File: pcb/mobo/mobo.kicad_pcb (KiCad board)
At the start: 2 copper layers, 51.6 x 89 mm, 70 parts, among them J1 ISP, J2 PEEL_MOTOR, J3 DRIVE_MOTOR, J4 SW1, J5 SPRING_FINGERS, J6 SW2, J8 USART1, U1 ATmega328P-A, U2 ATmega328P-M, U4 AP1117-50, U5 MC34063AD, U6 SP308xE, U7 DRV8837, U8 DRV8837, Y1 16MHz

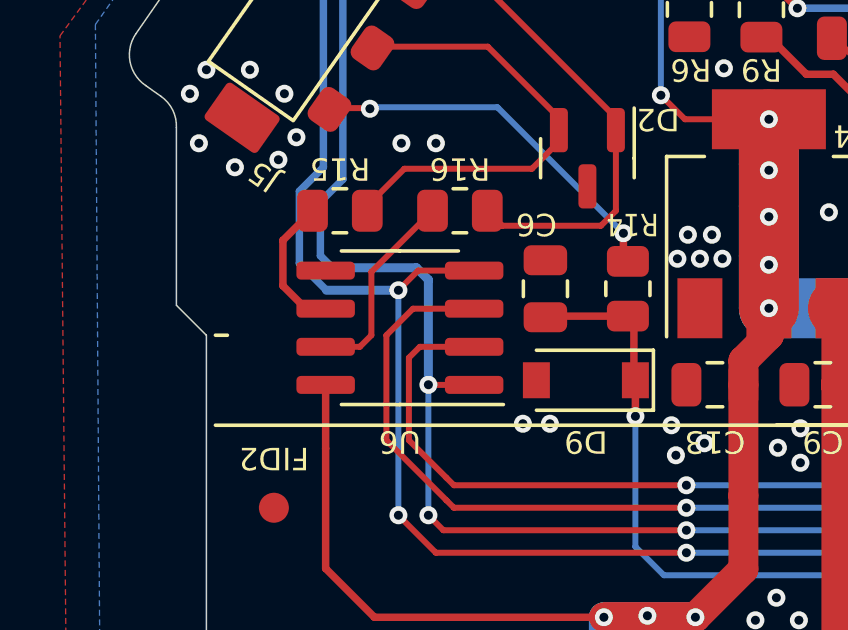
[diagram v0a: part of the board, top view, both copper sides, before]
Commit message: Add decoupling cap for RS-485 transceiver, Set edge clearance to 0.2mm
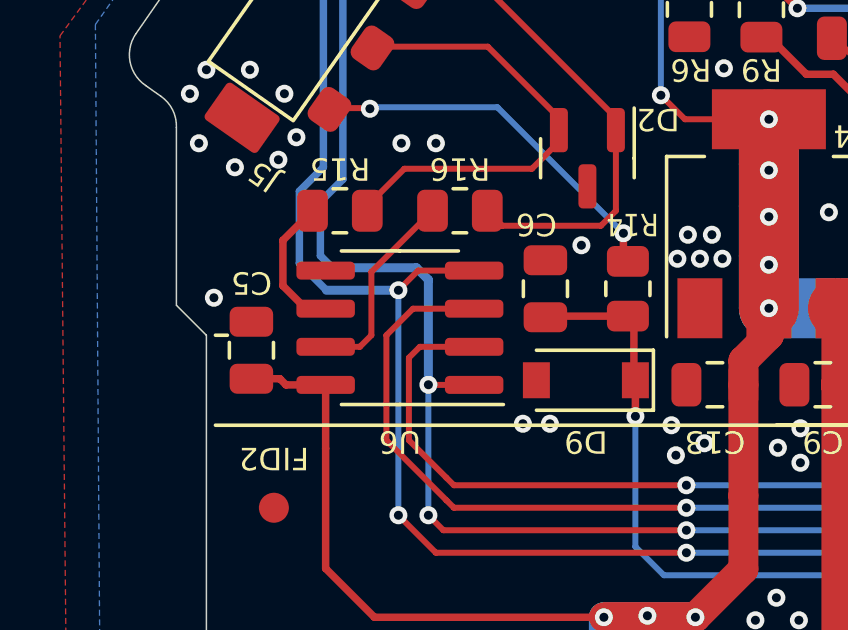
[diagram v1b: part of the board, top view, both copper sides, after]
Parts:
- added C5: 100n, Capacitor_SMD:C_0805_2012Metric, F.Cu at (103.8, 50.3)
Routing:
- net +5V: track 244.5 -> 247.0 mm
- net GND: vias 115 -> 117
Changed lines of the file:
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@@
     )
   )
+  (footprint "Capacitor_SMD:C_0805_2012Metric" (layer "F.Cu")
+    (at 103.8 50.3 -90)
+    (descr "Capacitor SMD 0805 (2012 Metric), square (rectangular) end terminal, IPC_7351 nominal, (Body size source: IPC-SM-782 page 76, https://www.pcb-3d.com/wordpress/wp-content/uploads/ipc-sm-782a_amendment_1_and_2.pdf, https://docs.google.com/spreadsheets/d/1BsfQQcO9C6DZCsRaXUlFlo91Tg2WpOkGARC1WS5S8t0/edit?usp=sharing), generated with kicad-footprint-generator")
+    (tags "capacitor")
+    (property "JLCPCB" "C49678")
+    (property "LCSC" "C476766")
+    (property "Sheetfile" "mobo.kicad_sch")
+    (property "Sheetname" "")
+    (property "ki_description" "Unpolarized capacitor, small symbol")
+    (property "ki_keywords" "capacitor cap")
+    (attr smd)
+    (fp_text reference "C5" (at -2.25 0 -180 unlocked) (layer "F.SilkS")
+        (effects (font (size 0.75 0.75) (thickness 0.1)))
+    )
+    (fp_text value "100n" (at 0 1.68 90) (layer "F.Fab")
+        (effects (font (size 1 1) (thickness 0.15)))
+    )
+    (fp_text user "${REFERENCE}" (at 0 0 90) (layer "F.Fab")
+        (effects (font (size 0.5 0.5) (thickness 0.08)))
+    )
+    (fp_line (start -0.261252 -0.735) (end 0.261252 -0.735)
+      (stroke (width 0.12) (type solid)) (layer "F.SilkS"))
+    (fp_line (start -0.261252 0.735) (end 0.261252 0.735)
+      (stroke (width 0.12) (type solid)) (layer "F.SilkS"))
+    (fp_line (start -1.7 -0.98) (end 1.7 -0.98)
+      (stroke (width 0.05) (type solid)) (layer "F.CrtYd"))
+    (fp_line (start -1.7 0.98) (end -1.7 -0.98)
+      (stroke (width 0.05) (type solid)) (layer "F.CrtYd"))
+    (fp_line (start 1.7 -0.98) (end 1.7 0.98)
+      (stroke (width 0.05) (type solid)) (layer "F.CrtYd"))
+    (fp_line (start 1.7 0.98) (end -1.7 0.98)
+      (stroke (width 0.05) (type solid)) (layer "F.CrtYd"))
+    (fp_line (start -1 -0.625) (end 1 -0.625)
+      (stroke (width 0.1) (type solid)) (layer "F.Fab"))
+    (fp_line (start -1 0.625) (end -1 -0.625)
+      (stroke (width 0.1) (type solid)) (layer "F.Fab"))
+    (fp_line (start 1 -0.625) (end 1 0.625)
+      (stroke (width 0.1) (type solid)) (layer "F.Fab"))
+    (fp_line (start 1 0.625) (end -1 0.625)
+      (stroke (width 0.1) (type solid)) (layer "F.Fab"))
+    (pad "1" smd roundrect (at -0.95 0 270) (size 1 1.45) (layers "F.Cu" "F.Paste" "F.Mask") (roundrect_rratio 0.25)
+      (net 1 "GND") (pintype "passive"))
+    (pad "2" smd roundrect (at 0.95 0 270) (size 1 1.45) (layers "F.Cu" "F.Paste" "F.Mask") (roundrect_rratio 0.25)
+      (net 11 "+5V") (pintype "passive"))
+    (model "${KICAD6_3DMODEL_DIR}/Capacitor_SMD.3dshapes/C_0805_2012Metric.wrl"
+      (offset (xyz 0 0 0))
+      (scale (xyz 1 1 1))
+      (rotate (xyz 0 0 0))
+    )
+  )
   (footprint "Connector_Molex:Molex_PicoBlade_53261-0271_1x02-1MP_P1.25mm_Horizontal" (layer "F.Cu")
     (at 119.2 69.5 180)
@@
   (via (at 133.2 102.7) (size 0.6) (drill 0.3) (layers "F.Cu" "B.Cu") (free) (net 1))
   (via (at 101.75 41.75) (size 0.6) (drill 0.3) (layers "F.Cu" "B.Cu") (free) (net 1))
+  (via (at 102.55 48.55) (size 0.6) (drill 0.3) (layers "F.Cu" "B.Cu") (free) (net 1))
   (via (at 110.55 34.6) (size 0.6) (drill 0.3) (layers "F.Cu" "B.Cu") (free) (net 1))
   (via (at 122.1 52.9) (size 0.6) (drill 0.3) (layers "F.Cu" "B.Cu") (free) (net 1))
@@
   (via (at 130.3 65.55) (size 0.6) (drill 0.3) (layers "F.Cu" "B.Cu") (free) (net 1))
   (via (at 112.3 64.55) (size 0.6) (drill 0.3) (layers "F.Cu" "B.Cu") (free) (net 1))
+  (via (at 114.8 46.8) (size 0.6) (drill 0.3) (layers "F.Cu" "B.Cu") (free) (net 1))
   (via (at 136.9 47.6) (size 0.6) (drill 0.3) (layers "F.Cu" "B.Cu") (free) (net 1))
   (segment (start 143.950001 54.700001) (end 143.950001 56.245) (width 0.2) (layer "F.Cu") (net 2))
@@
   (segment (start 138.616942 74.55) (end 139.3 74.55) (width 0.2) (layer "F.Cu") (net 11))
   (segment (start 106.275 51.455) (end 106.275 53.575) (width 0.25) (layer "F.Cu") (net 11))
+  (segment (start 104.75 51.25) (end 103.8 51.25) (width 0.25) (layer "F.Cu") (net 11))
   (segment (start 121.05 49.8) (end 121.05 48.9) (width 1) (layer "F.Cu") (net 11))
   (segment (start 127 102.2) (end 128.55 100.65) (width 0.5) (layer "F.Cu") (net 11))
@@
   (segment (start 132.6125 72.3) (end 131.95 72.3) (width 0.3) (layer "F.Cu") (net 11))
   (segment (start 132.6125 73.3) (end 132.086396 73.3) (width 0.3) (layer "F.Cu") (net 11))
+  (segment (start 106.275 51.455) (end 104.955 51.455) (width 0.25) (layer "F.Cu") (net 11))
   (segment (start 121.95 77.8) (end 121.95 77.7) (width 0.3) (layer "F.Cu") (net 11))
   (segment (start 121.95 77.7) (end 120.8 76.55) (width 0.3) (layer "F.Cu") (net 11))
@@
   (segment (start 115.55 76.55) (end 115.55 74.9) (width 1) (layer "F.Cu") (net 11))
   (segment (start 130.125 114.125) (end 130.425 114.125) (width 0.2) (layer "F.Cu") (net 11))
+  (segment (start 104.955 51.455) (end 104.75 51.25) (width 0.25) (layer "F.Cu") (net 11))
   (segment (start 140.8 76.05) (end 140.8 74.95) (width 0.5) (layer "F.Cu") (net 11))
   (segment (start 128.5 57) (end 128.5 56.1) (width 1) (layer "F.Cu") (net 11))

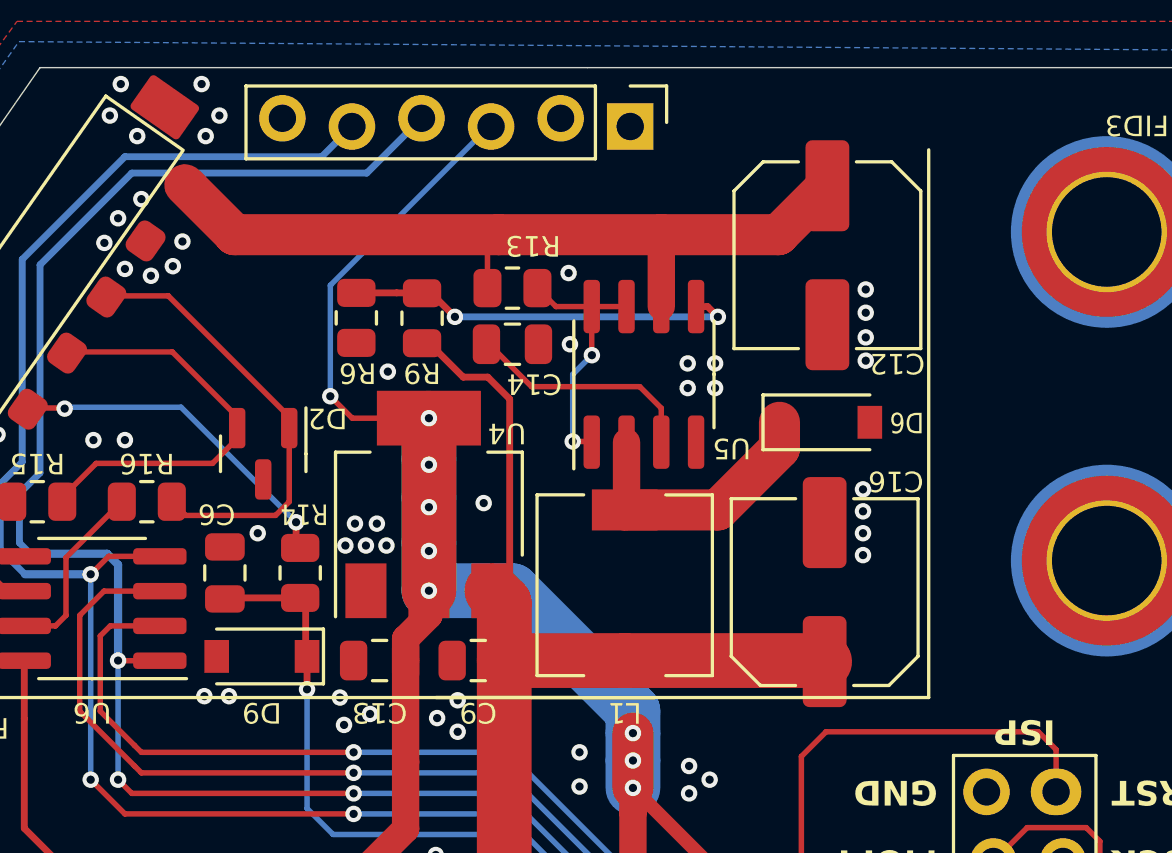
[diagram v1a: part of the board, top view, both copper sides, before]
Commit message: Add diode for reverse polarity protection, Add SMPS bypass jumper
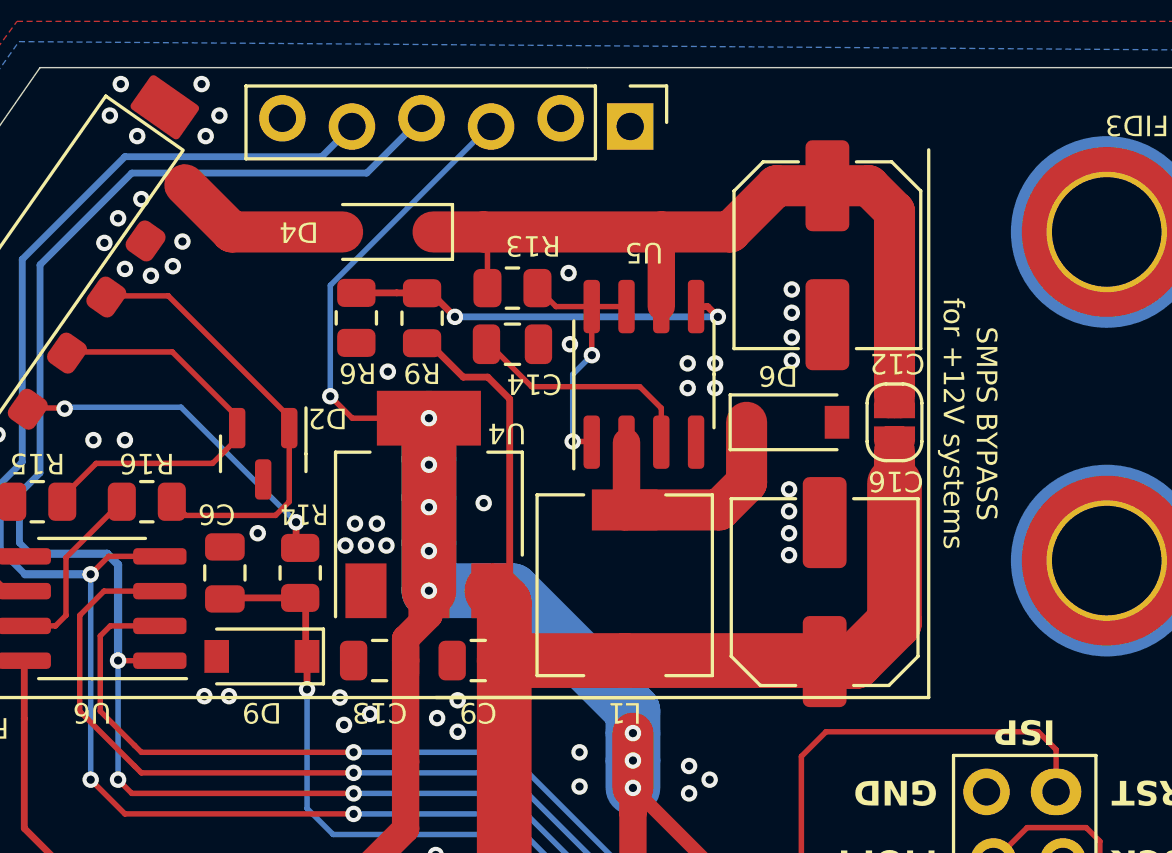
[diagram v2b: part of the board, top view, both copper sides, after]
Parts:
- added D4: 1N5819, Diode_SMD:D_SOD-123, F.Cu at (119.5, 35.8)
- added JP2: BYPASS_SMPS, Jumper:SolderJumper-2_P1.3mm_Open_RoundedPad1.0x1.5mm, F.Cu at (138.1, 42.8)
- moved D6 1.20 mm to (134.3, 42.8)
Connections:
- J5 pad 1: +VDC -> Net-(D4-A)
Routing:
- net +10V: track 86.0 -> 95.8 mm
- net Net-(D4-A): track 0.00 -> 6.47 mm
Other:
- board text added: "SMPS BYPASS for +12V systems"

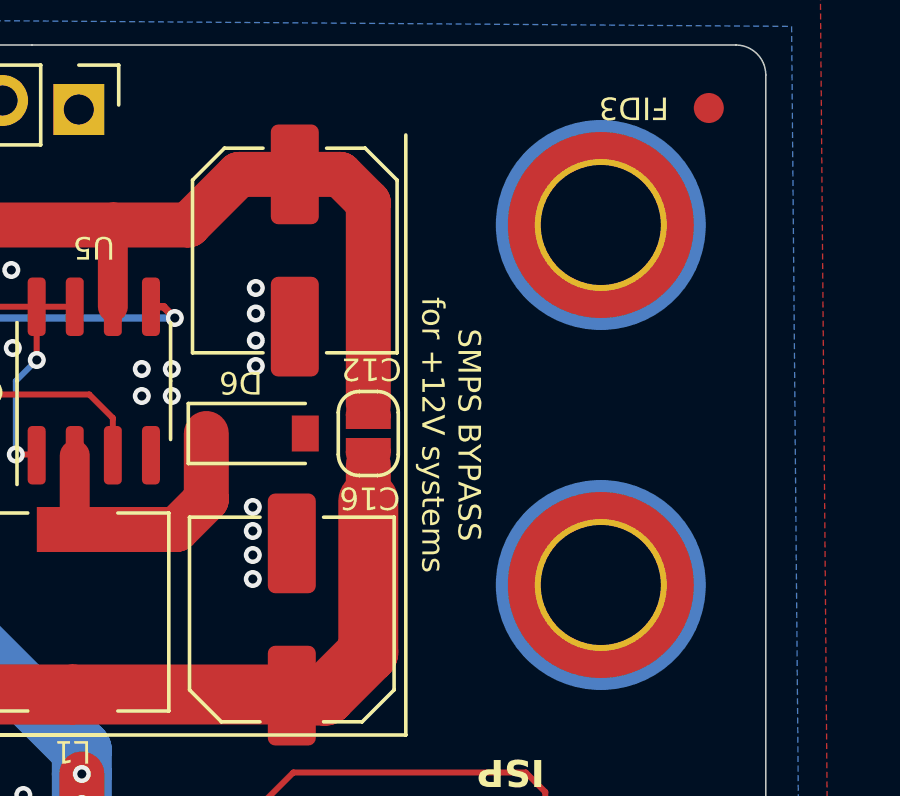
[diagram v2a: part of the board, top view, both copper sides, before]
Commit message: Replace bypass jumper with 0R resistor
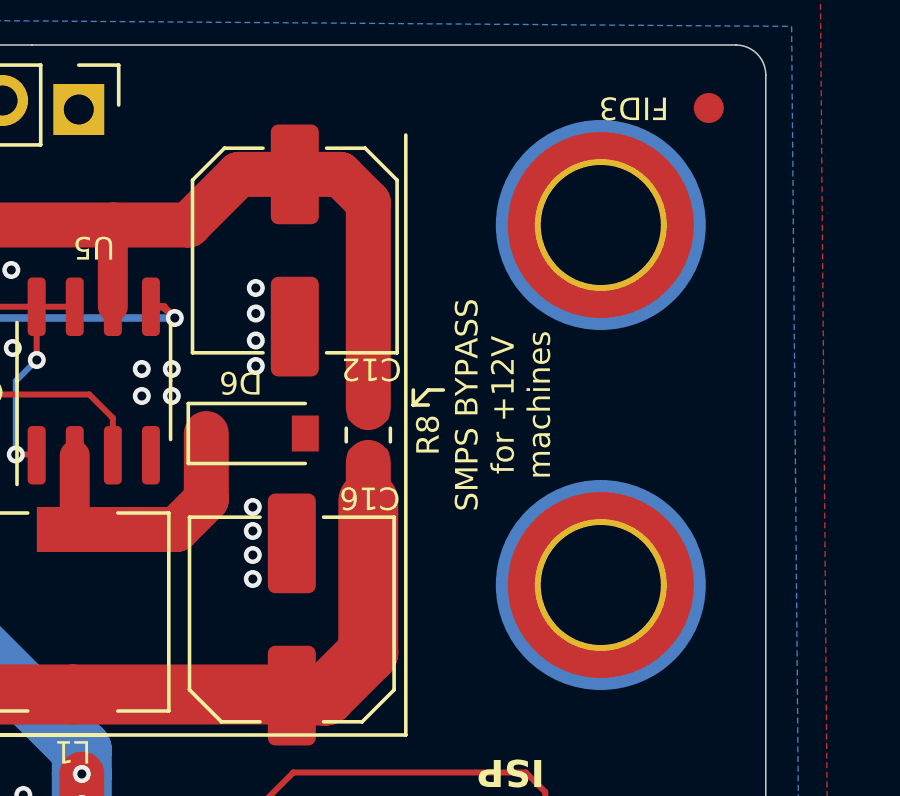
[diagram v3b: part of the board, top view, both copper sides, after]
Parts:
- removed JP2: BYPASS_SMPS, Jumper:SolderJumper-2_P1.3mm_Open_RoundedPad1.0x1.5mm
- added R8: BYPASS_SMPS, Resistor_SMD:R_0805_2012Metric, F.Cu at (138.1, 42.8)
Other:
- board text added: "SMPS BYPASS for +12V machines"
- board text removed: "SMPS BYPASS for +12V systems"

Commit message: Cleanup tracks and vias
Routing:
- net DRIVE_QUAD_B: track 51.8 -> 50.6 mm
- net +5V: track 247.0 -> 245.9 mm
- net LED_G: track 45.9 -> 44.8 mm
- net OSC_IN: track 12.1 -> 11.1 mm
- net RS-485+: track 15.5 -> 14.5 mm
- net SW1: track 46.7 -> 46.0 mm
- net MOPI: track 36.1 -> 35.5 mm
- net PEEL2: track 24.4 -> 23.8 mm
- net MCU_TX: track 71.8 -> 71.1 mm
- net Net-(U6-A): track 4.65 -> 3.99 mm

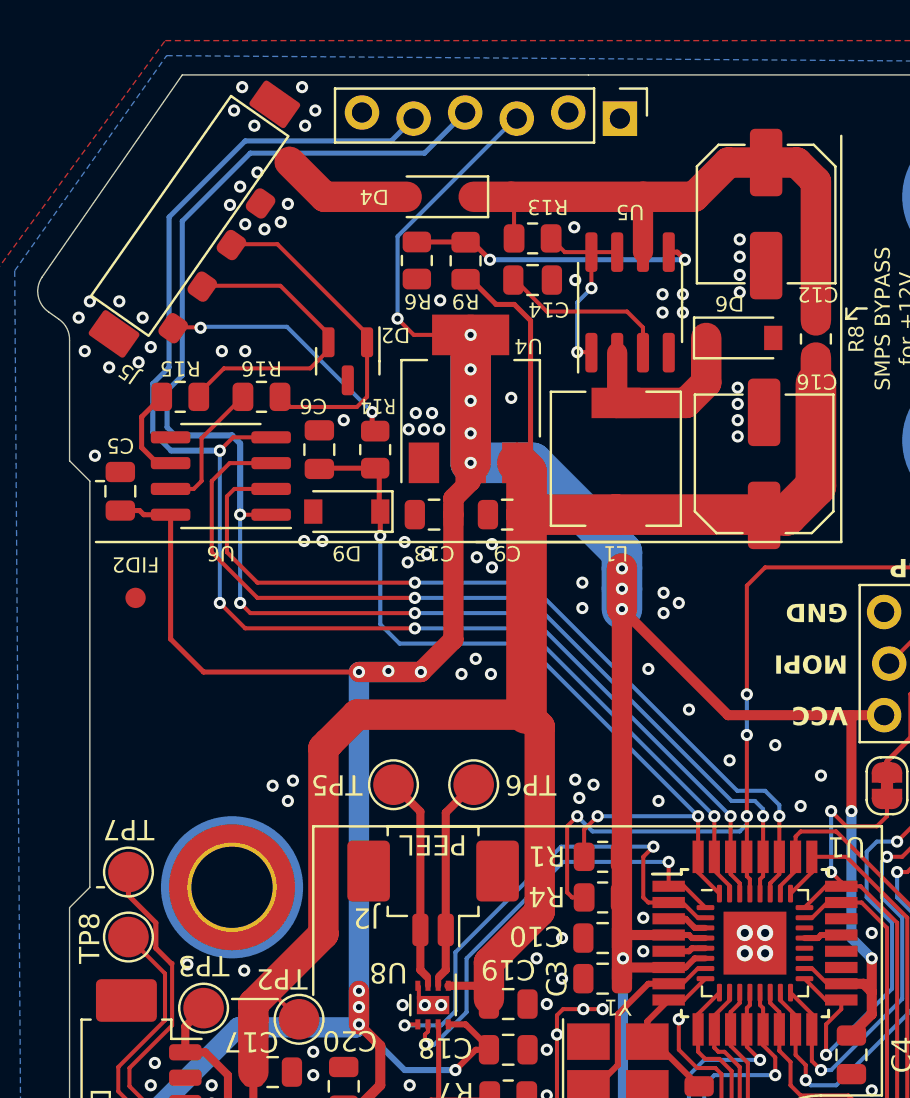
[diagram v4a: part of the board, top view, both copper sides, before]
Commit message: Replace ATmega328P with ATmega328PB and improve RS-485 routing
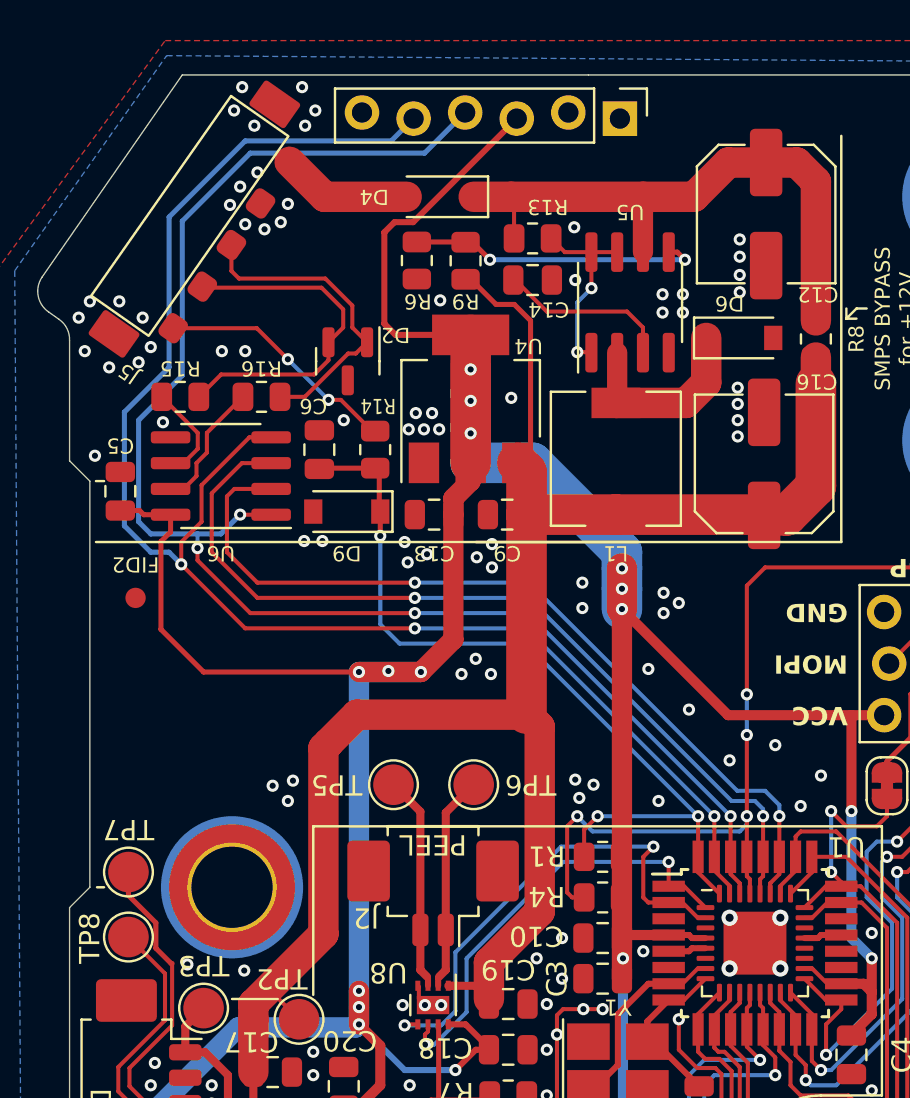
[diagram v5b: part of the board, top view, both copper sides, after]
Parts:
- U1: value ATmega328P-A -> ATmega328PB-A
- U2: value ATmega328P-M -> ATmega328PB-M
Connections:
- net Net-(U6-A) renamed /DRV_RS-485+
- net Net-(U6-B) renamed /DRV_RS-485-
- U1 pad 3: GND -> unconnected-(U1-PE0-Pad3)
- U1 pad 6: +5V -> unconnected-(U1-PE1-Pad6)
- U2 pad 3: GND -> unconnected-(U2-PE0-Pad3)
- U2 pad 6: +5V -> unconnected-(U2-PE1-Pad6)
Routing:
- net MCU_TX: track 71.1 -> 77.3 mm, vias 4 -> 3
- net +5V: track 245.9 -> 242.0 mm, vias 22 -> 19
- net RS-485+: track 14.5 -> 17.3 mm
- net MCU_RX: track 73.1 -> 75.8 mm
- net GND: track 32.4 -> 30.4 mm
- net /DRV_RS-485-: track 6.68 -> 5.75 mm
- net Net-(J5-Pin_5): track 12.4 -> 11.9 mm
- net RS-485-: track 16.0 -> 15.4 mm
